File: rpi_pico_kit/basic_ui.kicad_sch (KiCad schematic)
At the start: 30 parts, among them Q3 DMN63D8L-7, Q4 DMN63D8L-7, Q5 DMN63D8L-7, Q6 DMN63D8L-7, SW2 RotaryEncoder_Switch, SW3 SW_Push, SW4 SW_Push, SW5 SW_Push, SW6 SW_Push, U6 74HC14

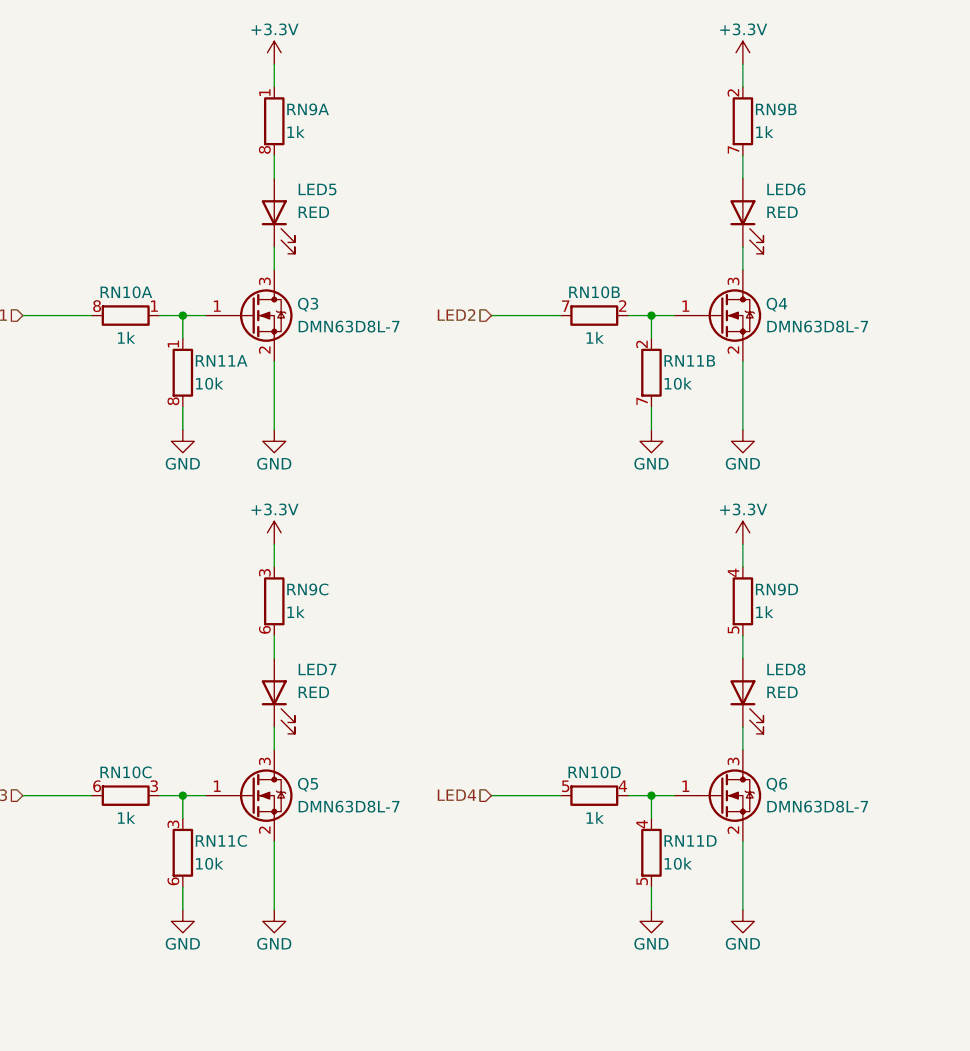
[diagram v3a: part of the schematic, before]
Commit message: basic leds (unrouted 295)
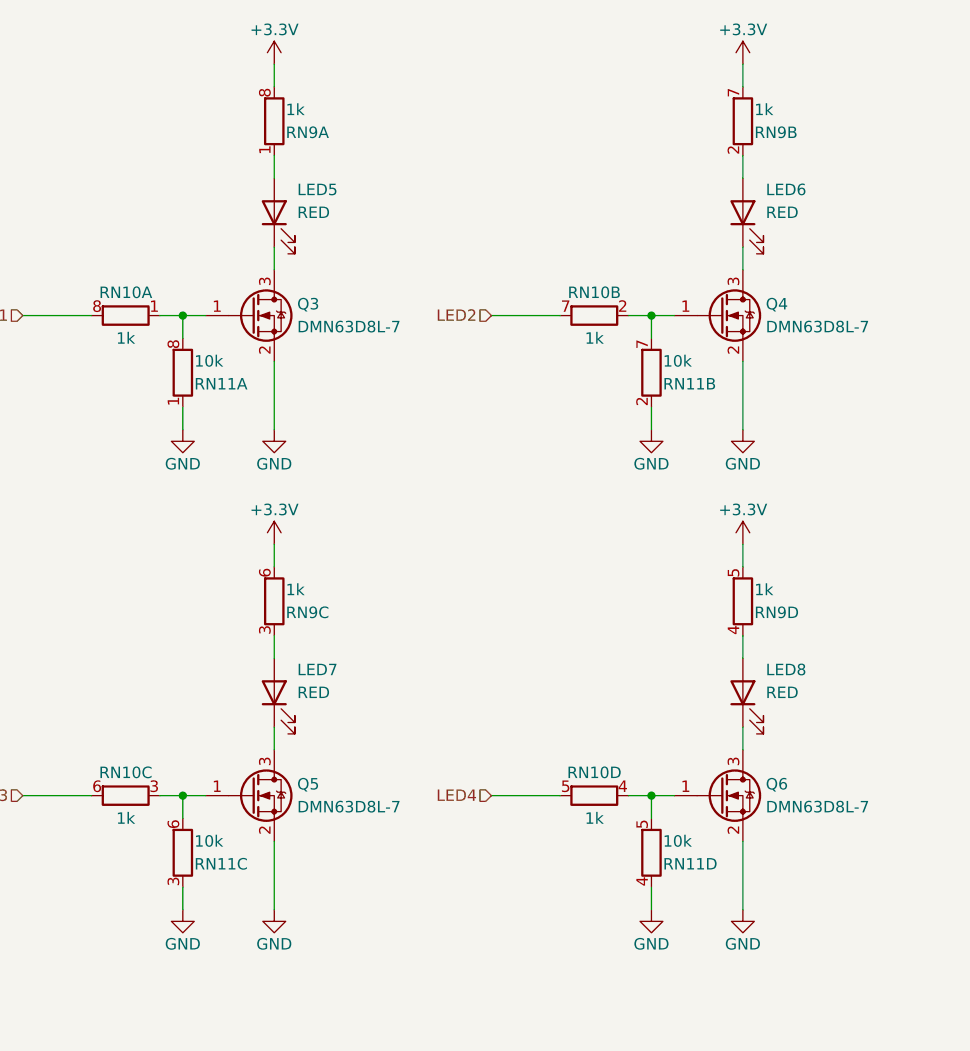
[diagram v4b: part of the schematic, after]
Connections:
- net +3V3: now also RN9.5 (R4.2), RN9.6 (R3.2), RN9.7 (R2.2), RN9.8 (R1.2); no longer RN9.1 (R1.1), RN9.2 (R2.1), RN9.3 (R3.1), RN9.4 (R4.1)
- net GND: now also RN11.1 (R1.1), RN11.2 (R2.1), RN11.3 (R3.1), RN11.4 (R4.1); no longer RN11.5 (R4.2), RN11.6 (R3.2), RN11.7 (R2.2), RN11.8 (R1.2)
- net at LED5.2 (A): now also RN9.1 (R1.1); no longer RN9.8 (R1.2)
- net at Q4.1 (G), RN10.2 (R2.1): now also RN11.7 (R2.2); no longer RN11.2 (R2.1)
- net at Q5.1 (G), RN10.3 (R3.1): now also RN11.6 (R3.2); no longer RN11.3 (R3.1)
- net at LED6.2 (A): now also RN9.2 (R2.1); no longer RN9.7 (R2.2)
- net at Q6.1 (G), RN10.4 (R4.1): now also RN11.5 (R4.2); no longer RN11.4 (R4.1)
- net at Q3.1 (G), RN10.1 (R1.1): now also RN11.8 (R1.2); no longer RN11.1 (R1.1)
- net at LED7.2 (A): now also RN9.3 (R3.1); no longer RN9.6 (R3.2)
- net at LED8.2 (A): now also RN9.4 (R4.1); no longer RN9.5 (R4.2)
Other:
- moved on the sheet: RN11A, RN11B, RN11C, RN11D, RN9A, RN9B, RN9C, RN9D
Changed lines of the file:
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@@
     (pin "3")
   )
-  (symbol (lib_id "Device:R_Pack04_Split") (at 107.95 26.67 180) (unit 2)
-    (in_bom yes) (on_board yes)
-    (property "Reference" "RN9" (id 0) (at 109.22 25.4 0)
-      (effects (font (size 1.27 1.27)) (justify right))
-    )
-    (property "Value" "1k" (id 1) (at 109.22 27.94 0)
+  (symbol (lib_id "Device:R_Pack04_Split") (at 107.95 26.67 0) (mirror y) (unit 2)
+    (in_bom yes) (on_board yes)
+    (property "Reference" "RN9" (id 0) (at 109.22 27.94 0)
+      (effects (font (size 1.27 1.27)) (justify right))
+    )
+    (property "Value" "1k" (id 1) (at 109.22 25.4 0)
       (effects (font (size 1.27 1.27)) (justify right))
     )
@@
     (pin "1")
   )
-  (symbol (lib_id "Device:R_Pack04_Split") (at 45.72 54.61 180) (unit 1)
-    (in_bom yes) (on_board yes)
-    (property "Reference" "RN11" (id 0) (at 46.99 53.34 0)
-      (effects (font (size 1.27 1.27)) (justify right))
-    )
-    (property "Value" "10k" (id 1) (at 46.99 55.88 0)
+  (symbol (lib_id "Device:R_Pack04_Split") (at 45.72 54.61 0) (mirror y) (unit 1)
+    (in_bom yes) (on_board yes)
+    (property "Reference" "RN11" (id 0) (at 46.99 55.88 0)
+      (effects (font (size 1.27 1.27)) (justify right))
+    )
+    (property "Value" "10k" (id 1) (at 46.99 53.34 0)
       (effects (font (size 1.27 1.27)) (justify right))
     )
@@
     (pin "1")
   )
-  (symbol (lib_id "Device:R_Pack04_Split") (at 97.79 107.95 180) (unit 4)
-    (in_bom yes) (on_board yes)
-    (property "Reference" "RN11" (id 0) (at 99.06 106.68 0)
-      (effects (font (size 1.27 1.27)) (justify right))
-    )
-    (property "Value" "10k" (id 1) (at 99.06 109.22 0)
+  (symbol (lib_id "Device:R_Pack04_Split") (at 97.79 107.95 0) (mirror y) (unit 4)
+    (in_bom yes) (on_board yes)
+    (property "Reference" "RN11" (id 0) (at 99.06 109.22 0)
+      (effects (font (size 1.27 1.27)) (justify right))
+    )
+    (property "Value" "10k" (id 1) (at 99.06 106.68 0)
       (effects (font (size 1.27 1.27)) (justify right))
     )
@@
     (pin "1")
   )
-  (symbol (lib_id "Device:R_Pack04_Split") (at 107.95 80.01 180) (unit 4)
-    (in_bom yes) (on_board yes)
-    (property "Reference" "RN9" (id 0) (at 109.22 78.74 0)
-      (effects (font (size 1.27 1.27)) (justify right))
-    )
-    (property "Value" "1k" (id 1) (at 109.22 81.28 0)
+  (symbol (lib_id "Device:R_Pack04_Split") (at 107.95 80.01 0) (mirror y) (unit 4)
+    (in_bom yes) (on_board yes)
+    (property "Reference" "RN9" (id 0) (at 109.22 81.28 0)
+      (effects (font (size 1.27 1.27)) (justify right))
+    )
+    (property "Value" "1k" (id 1) (at 109.22 78.74 0)
       (effects (font (size 1.27 1.27)) (justify right))
     )
@@
     (pin "7")
   )
-  (symbol (lib_id "Device:R_Pack04_Split") (at 97.79 54.61 180) (unit 2)
-    (in_bom yes) (on_board yes)
-    (property "Reference" "RN11" (id 0) (at 99.06 53.34 0)
-      (effects (font (size 1.27 1.27)) (justify right))
-    )
-    (property "Value" "10k" (id 1) (at 99.06 55.88 0)
+  (symbol (lib_id "Device:R_Pack04_Split") (at 97.79 54.61 0) (mirror y) (unit 2)
+    (in_bom yes) (on_board yes)
+    (property "Reference" "RN11" (id 0) (at 99.06 55.88 0)
+      (effects (font (size 1.27 1.27)) (justify right))
+    )
+    (property "Value" "10k" (id 1) (at 99.06 53.34 0)
       (effects (font (size 1.27 1.27)) (justify right))
     )
@@
     (pin "7")
   )
-  (symbol (lib_id "Device:R_Pack04_Split") (at 45.72 107.95 180) (unit 3)
-    (in_bom yes) (on_board yes)
-    (property "Reference" "RN11" (id 0) (at 46.99 106.68 0)
-      (effects (font (size 1.27 1.27)) (justify right))
-    )
-    (property "Value" "10k" (id 1) (at 46.99 109.22 0)
+  (symbol (lib_id "Device:R_Pack04_Split") (at 45.72 107.95 0) (mirror y) (unit 3)
+    (in_bom yes) (on_board yes)
+    (property "Reference" "RN11" (id 0) (at 46.99 109.22 0)
+      (effects (font (size 1.27 1.27)) (justify right))
+    )
+    (property "Value" "10k" (id 1) (at 46.99 106.68 0)
       (effects (font (size 1.27 1.27)) (justify right))
     )
@@
     (pin "2")
   )
-  (symbol (lib_id "Device:R_Pack04_Split") (at 55.88 80.01 180) (unit 3)
-    (in_bom yes) (on_board yes)
-    (property "Reference" "RN9" (id 0) (at 57.15 78.74 0)
-      (effects (font (size 1.27 1.27)) (justify right))
-    )
-    (property "Value" "1k" (id 1) (at 57.15 81.28 0)
+  (symbol (lib_id "Device:R_Pack04_Split") (at 55.88 80.01 0) (mirror y) (unit 3)
+    (in_bom yes) (on_board yes)
+    (property "Reference" "RN9" (id 0) (at 57.15 81.28 0)
+      (effects (font (size 1.27 1.27)) (justify right))
+    )
+    (property "Value" "1k" (id 1) (at 57.15 78.74 0)
       (effects (font (size 1.27 1.27)) (justify right))
     )
@@
     (pin "6")
   )
-  (symbol (lib_id "Device:R_Pack04_Split") (at 55.88 26.67 180) (unit 1)
-    (in_bom yes) (on_board yes)
-    (property "Reference" "RN9" (id 0) (at 57.15 25.4 0)
-      (effects (font (size 1.27 1.27)) (justify right))
-    )
-    (property "Value" "1k" (id 1) (at 57.15 27.94 0)
-      (effects (font (size 1.27 1.27)) (justify right))
-    )
+  (symbol (lib_id "Device:R_Pack04_Split") (at 55.88 26.67 0) (mirror y) (unit 1)
+    (in_bom yes) (on_board yes)
+    (property "Reference" "RN9" (id 0) (at 57.15 27.94 0)
+      (effects (font (size 1.27 1.27)) (justify right))
+    )
+    (property "Value" "1k" (id 1) (at 57.15 25.4 0)
+      (effects (font (size 1.27 1.27)) (justify right))
+    )

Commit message: dac buttons (unrouted 270)
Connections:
- net GND: now also SW3.2, SW4.2, SW5.2, SW6.2; no longer SW3.1, SW4.1, SW5.1, SW6.1
- net at RN12.7 (R2.2), U6.3: now also SW4.1; no longer SW4.2
- net at RN12.6 (R3.2), U6.5: now also SW5.1; no longer SW5.2
- net at RN12.5 (R4.2), U6.9: now also SW6.1; no longer SW6.2
- net at RN12.8 (R1.2), U6.1: now also SW3.1; no longer SW3.2
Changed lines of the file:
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@@
     (effects (font (size 1.27 1.27)) (justify right))
   )
-  (symbol (lib_id "Switch:SW_Push") (at 153.67 59.69 0) (unit 1)
+  (symbol (lib_id "Switch:SW_Push") (at 153.67 59.69 0) (mirror y) (unit 1)
     (in_bom yes) (on_board yes)
     (property "Reference" "SW4" (id 0) (at 153.67 52.07 0)
@@
     (pin "6")
   )
-  (symbol (lib_id "Switch:SW_Push") (at 153.67 72.39 0) (unit 1)
+  (symbol (lib_id "Switch:SW_Push") (at 153.67 72.39 0) (mirror y) (unit 1)
     (in_bom yes) (on_board yes)
     (property "Reference" "SW5" (id 0) (at 153.67 64.77 0)
@@
     (pin "2")
   )
-  (symbol (lib_id "Switch:SW_Push") (at 153.67 85.09 0) (unit 1)
+  (symbol (lib_id "Switch:SW_Push") (at 153.67 85.09 0) (mirror y) (unit 1)
     (in_bom yes) (on_board yes)
     (property "Reference" "SW6" (id 0) (at 153.67 77.47 0)
@@
     (pin "1")
   )
-  (symbol (lib_id "Switch:SW_Push") (at 153.67 46.99 0) (unit 1)
+  (symbol (lib_id "Switch:SW_Push") (at 153.67 46.99 0) (mirror y) (unit 1)
     (in_bom yes) (on_board yes)
     (property "Reference" "SW3" (id 0) (at 153.67 39.37 0)

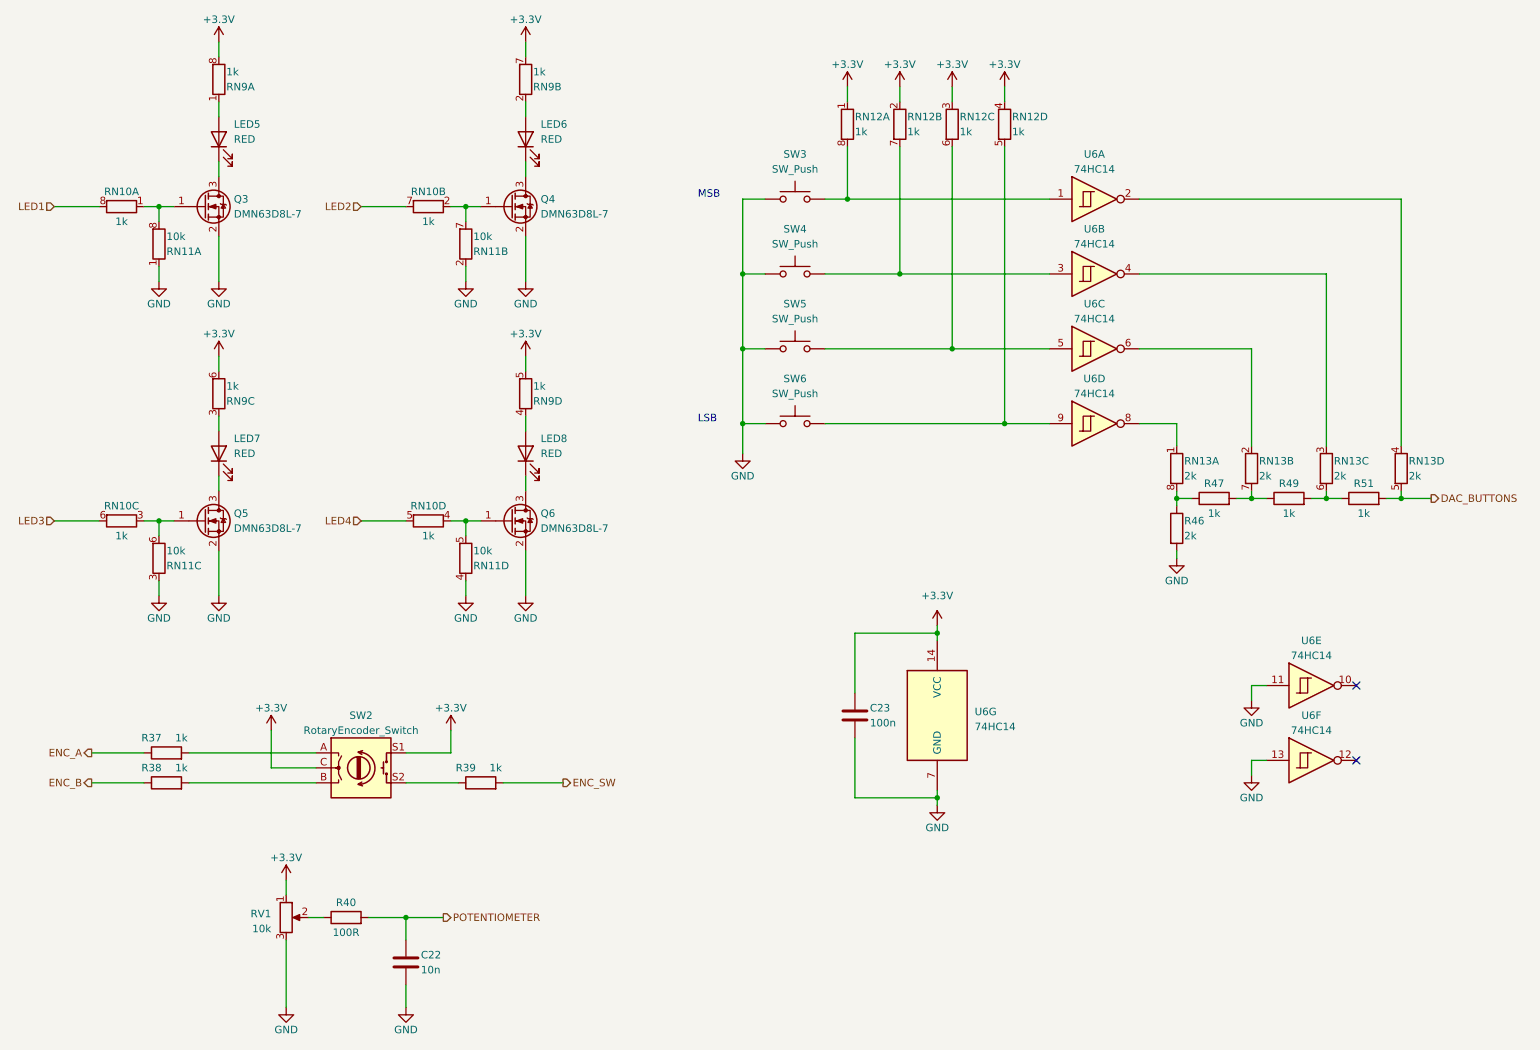
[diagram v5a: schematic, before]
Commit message: schematic cleared annotation
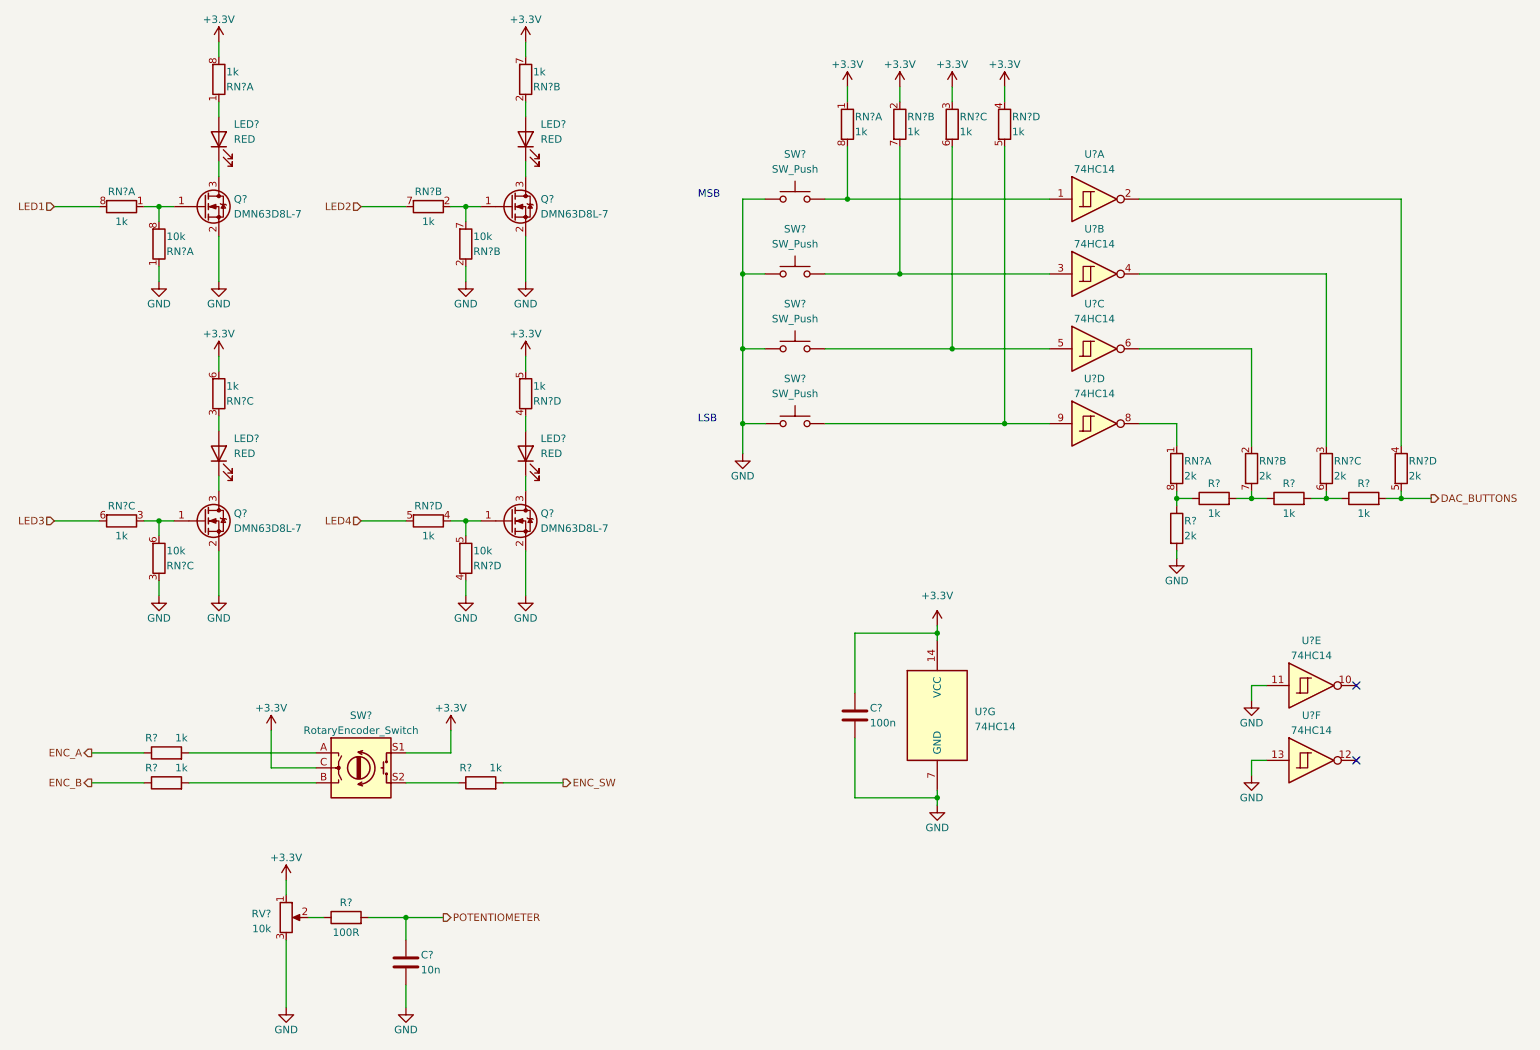
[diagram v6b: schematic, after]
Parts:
- renumbered C22 to C?, C23 to C?, LED5 to LED?, LED7 to LED?, LED6 to LED?, LED8 to LED?, Q4 to Q?, Q5 to Q?, Q3 to Q?, Q6 to Q?, R37 to R?, R40 to R?, R47 to R?, R51 to R?, R38 to R?, R46 to R?, R39 to R?, R49 to R?, RN12 to RN?, RN9 to RN?, RN10 to RN?, RN11 to RN?, RN13 to RN?, RV1 to RV?, SW4 to SW?, SW5 to SW?, SW6 to SW?, SW2 to SW?, SW3 to SW?, U6 to U?

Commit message: renumbered parts
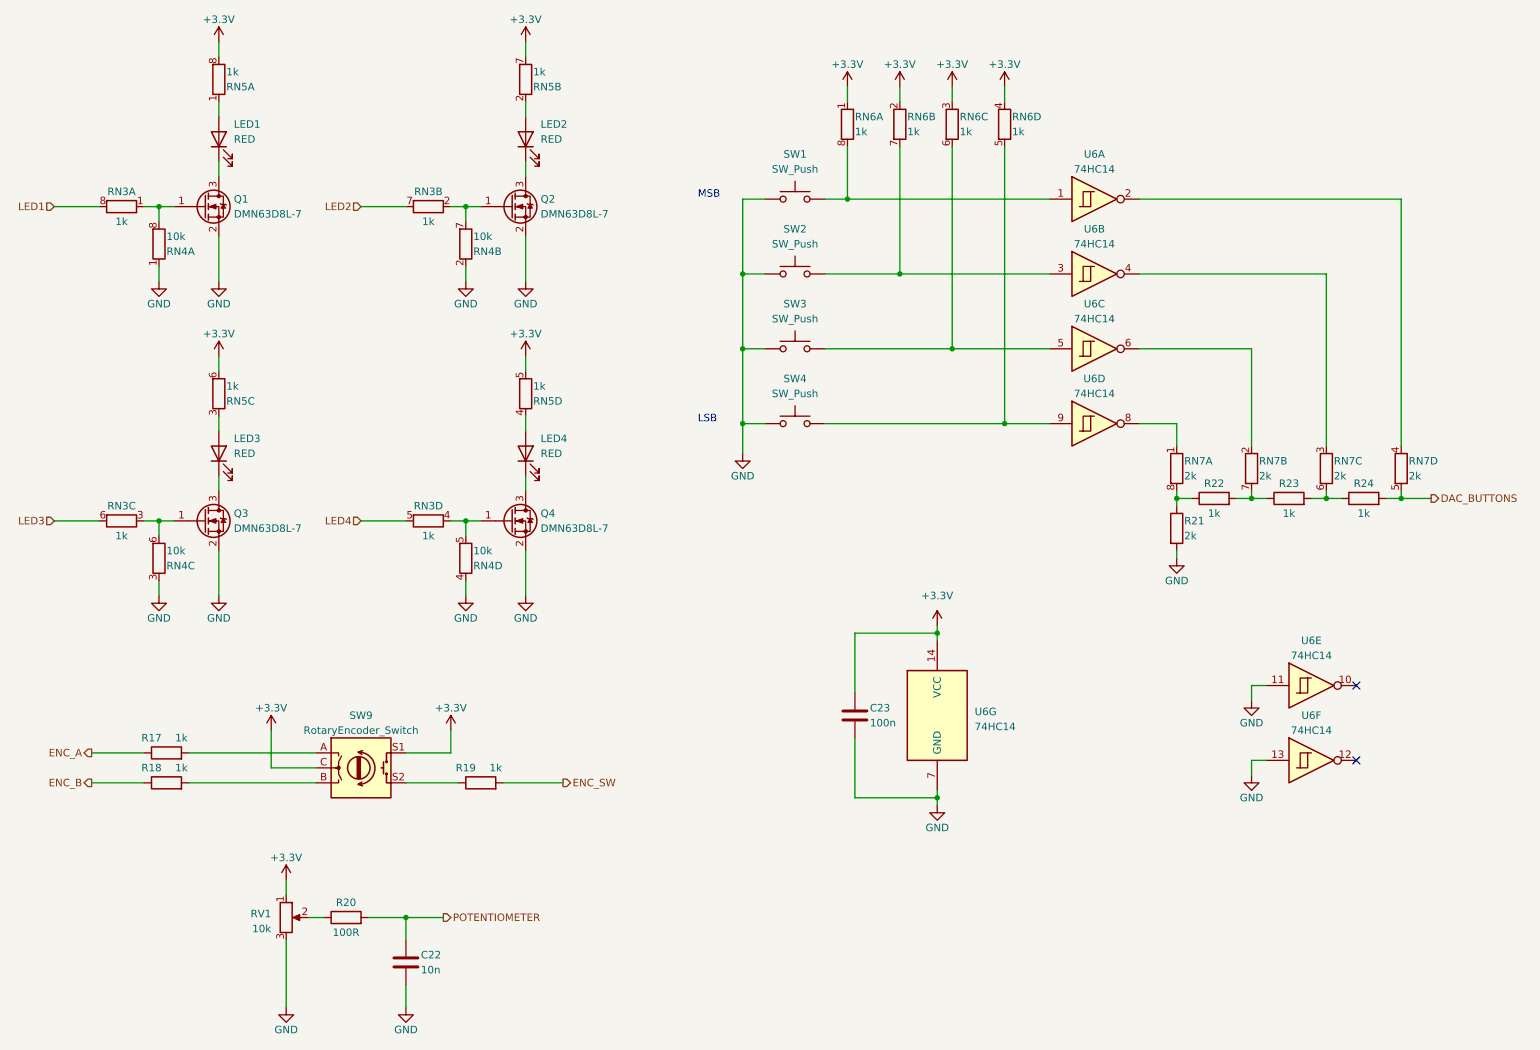
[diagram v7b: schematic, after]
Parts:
- gave numbers to parts that had none: 30
